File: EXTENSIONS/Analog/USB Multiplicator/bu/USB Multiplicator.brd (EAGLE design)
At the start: 30 x 63 mm, 9 parts, among them X1 USB-A

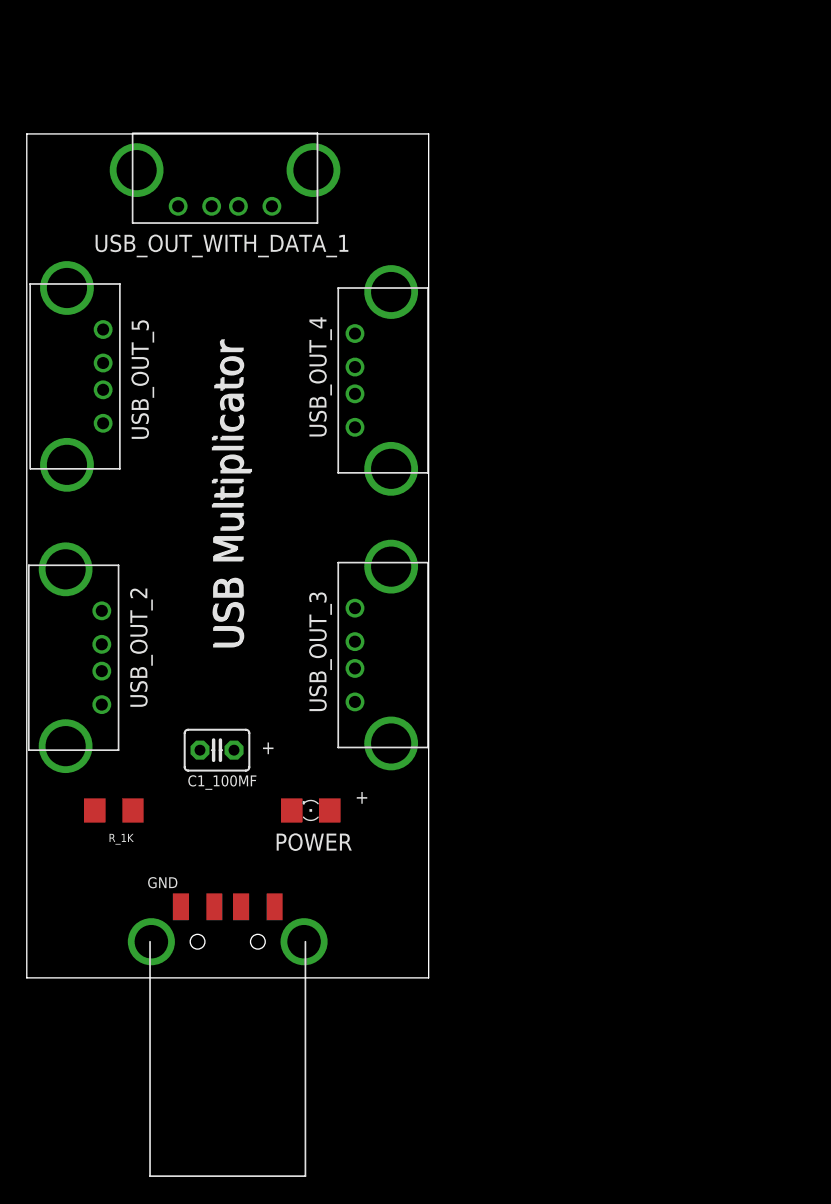
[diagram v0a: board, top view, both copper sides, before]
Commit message: Create v2 of USB Mutiplicator, make the board larger and 6 usb out
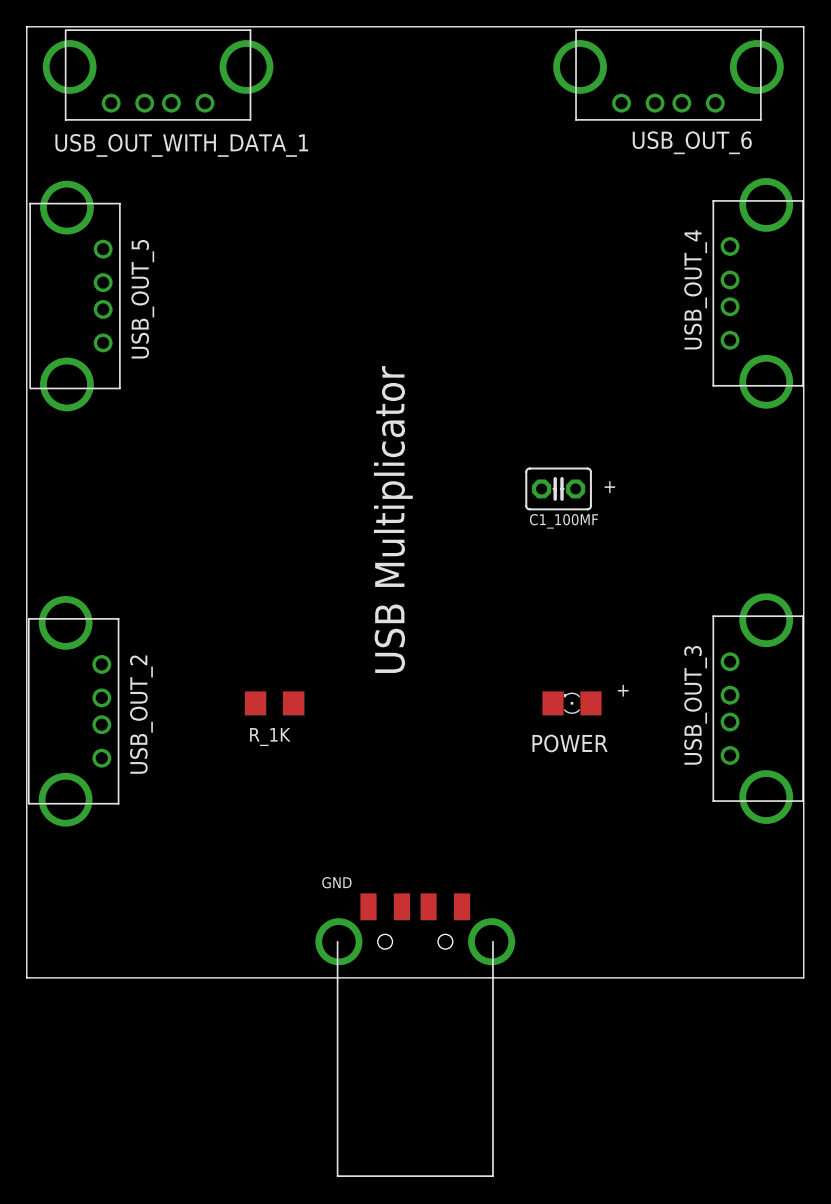
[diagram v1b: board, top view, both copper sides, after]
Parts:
- added USB_OUT_6: USB, STUNTAZ:USB-FEMALE-A-PTH
- moved C1_100MF 32.1 mm to (41.7, 48.5)
- moved USB_OUT_4 28.7 mm to (53.2, 70.0)
- moved USB_OUT_3 28.3 mm to (53.2, 39.0)
- moved LED_PWR 21.1 mm to (42.7, 32.5)
- moved R_1K 14.4 mm to (20.5, 32.5)
- moved X1 14.0 mm to (31.0, 14.7)
- moved USB_OUT_WITH_DATA_1 9.18 mm to (4.90, 76.0)
- moved USB_OUT_5 6.00 mm to (9.00, 56.0)
- moved USB_OUT_2 4.00 mm to (8.90, 25.0)
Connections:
- net GND: now also USB_OUT_6.GND
- net VCC: now also USB_OUT_6.VBUS
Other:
- board size 30 x 63 mm -> 58 x 71 mm
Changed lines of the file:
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@@
 <board>
 <plain>
-<wire x1="2" y1="12" x2="32" y2="12" width="0" layer="20"/>
-<wire x1="32" y1="12" x2="32" y2="75" width="0" layer="20"/>
-<wire x1="32" y1="75" x2="2" y2="75" width="0" layer="20"/>
-<wire x1="2" y1="75" x2="2" y2="12" width="0" layer="20"/>
+<wire x1="2" y1="12" x2="60" y2="12" width="0" layer="20"/>
+<wire x1="60" y1="12" x2="60" y2="83" width="0" layer="20"/>
+<wire x1="60" y1="83" x2="2" y2="83" width="0" layer="20"/>
+<wire x1="2" y1="83" x2="2" y2="12" width="0" layer="20"/>
 <text x="17" y="50.2" size="1.778" layer="26" rot="SMR90" align="center">USB Multiplicator
 MadeInTheUSB.net </text>
 <text x="22.5" y="18" size="1.27" layer="26" rot="MR90">PCBv2 - 2019.08</text>
-<text x="11" y="18.7" size="0.8128" layer="25">GND</text>
-<text x="19.5" y="28.7" size="1.016" layer="25">+</text>
-<text x="26.5" y="25" size="1.016" layer="25">+</text>
-<text x="20.5" y="21.5" size="1.27" layer="25">POWER</text>
-<text x="17" y="48" size="2.1844" layer="25" rot="R90" align="center">USB Multiplicator</text>
-<text x="17.1" y="48.1" size="2.1844" layer="25" rot="R90" align="center">USB Multiplicator</text>
+<text x="24" y="18.7" size="0.8128" layer="25">GND</text>
+<text x="45" y="48.2" size="1.016" layer="25">+</text>
+<text x="46" y="33" size="1.016" layer="25">+</text>
+<text x="42.5" y="29.5" size="1.27" layer="25" align="center">POWER</text>
+<text x="29.1" y="46.1" size="2.1844" layer="25" rot="R90" align="center">USB Multiplicator</text>
 </plain>
 <attributes>
@@
 </autorouter>
 <elements>
-<element name="X1" library="adafruit" package="MOLEX_480371000" value="USB-A" x="17" y="14.7" smashed="yes">
-<attribute name="VALUE" x="15.46" y="11.35" size="1.016" layer="27" font="vector"/>
-</element>
-<element name="C1_100MF" library="adafruit" package="C025-030X050" value="" x="16.2" y="29" smashed="yes">
-<attribute name="NAME" x="14" y="26.3" size="0.8128" layer="25" ratio="10"/>
-<attribute name="VALUE" x="13.914" y="25.952" size="1.27" layer="27" ratio="10"/>
-</element>
-<element name="LED_PWR" library="adafruit" package="1206" value="" x="23.2" y="24.5" smashed="yes" rot="R180">
-<attribute name="VALUE" x="24.47" y="27.04" size="1.27" layer="27" rot="R180"/>
-</element>
-<element name="R_1K" library="adafruit" package="R1206" value="" x="8.5" y="24.5" smashed="yes">
-<attribute name="NAME" x="8.103" y="22.143" size="0.6096" layer="25"/>
-<attribute name="VALUE" x="7.103" y="22.087" size="1.27" layer="27"/>
-</element>
-<element name="USB_OUT_WITH_DATA_1" library="STUNTAZ" package="USB-FEMALE-A-PTH" value="USB" x="9.9" y="68.3" smashed="yes">
-<attribute name="NAME" x="7" y="66.2" size="1.27" layer="25"/>
-</element>
-<element name="USB_OUT_2" library="STUNTAZ" package="USB-FEMALE-A-PTH" value="USB" x="8.9" y="29" smashed="yes" rot="R90">
-<attribute name="NAME" x="11" y="32.1" size="1.27" layer="25" rot="R90"/>
-</element>
-<element name="USB_OUT_3" library="STUNTAZ" package="USB-FEMALE-A-PTH" value="USB" x="25.2" y="43" smashed="yes" rot="R270">
-<attribute name="NAME" x="23.1" y="40.9" size="1.27" layer="25" rot="R270"/>
-</element>
-<element name="USB_OUT_4" library="STUNTAZ" package="USB-FEMALE-A-PTH" value="USB" x="25.2" y="63.5" smashed="yes" rot="R270">
-<attribute name="NAME" x="23.1" y="61.4" size="1.27" layer="25" rot="R270"/>
-</element>
-<element name="USB_OUT_5" library="STUNTAZ" package="USB-FEMALE-A-PTH" value="USB" x="9" y="50" smashed="yes" rot="R90">
-<attribute name="NAME" x="11.1" y="52.1" size="1.27" layer="25" rot="R90"/>
-</element>
+<element name="X1" library="adafruit" package="MOLEX_480371000" value="USB-A" x="31" y="14.7" smashed="yes">
+<attribute name="VALUE" x="29.46" y="11.35" size="1.016" layer="27" font="vector"/>
+</element>
+<element name="C1_100MF" library="adafruit" package="C025-030X050" value="" x="41.7" y="48.5" smashed="yes">
+<attribute name="NAME" x="39.5" y="45.8" size="0.8128" layer="25" ratio="10"/>
+<attribute name="VALUE" x="39.414" y="45.452" size="1.27" layer="27" ratio="10"/>
+</element>
+<element name="LED_PWR" library="adafruit" package="1206" value="" x="42.7" y="32.5" smashed="yes" rot="R180">
+<attribute name="VALUE" x="43.97" y="35.04" size="1.27" layer="27" rot="R180"/>
+</element>
+<element name="R_1K" library="adafruit" package="R1206" value="" x="20.5" y="32.5" smashed="yes">
+<attribute name="NAME" x="20.103" y="30.143" size="1.016" layer="25" align="center"/>
+<attribute name="VALUE" x="19.103" y="30.087" size="1.27" layer="27"/>
+</element>
+<element name="USB_OUT_WITH_DATA_1" library="STUNTAZ" package="USB-FEMALE-A-PTH" value="USB" x="4.9" y="76" smashed="yes">
+<attribute name="NAME" x="4" y="73.7" size="1.27" layer="25"/>
+</element>
+<element name="USB_OUT_2" library="STUNTAZ" package="USB-FEMALE-A-PTH" value="USB" x="8.9" y="25" smashed="yes" rot="R90">
+<attribute name="NAME" x="11" y="27.1" size="1.27" layer="25" rot="R90"/>
+</element>
+<element name="USB_OUT_3" library="STUNTAZ" package="USB-FEMALE-A-PTH" value="USB" x="53.2" y="39" smashed="yes" rot="R270">
+<attribute name="NAME" x="51.1" y="36.9" size="1.27" layer="25" rot="R270"/>
+</element>
+<element name="USB_OUT_4" library="STUNTAZ" package="USB-FEMALE-A-PTH" value="USB" x="53.2" y="70" smashed="yes" rot="R270">
+<attribute name="NAME" x="51.1" y="67.9" size="1.27" layer="25" rot="R270"/>
+</element>
+<element name="USB_OUT_5" library="STUNTAZ" package="USB-FEMALE-A-PTH" value="USB" x="9" y="56" smashed="yes" rot="R90">
+<attribute name="NAME" x="11.1" y="58.1" size="1.27" layer="25" rot="R90"/>
+</element>
+<element name="USB_OUT_6" library="STUNTAZ" package="USB-FEMALE-A-PTH" value="USB" x="43" y="76"/>
 </elements>
 <signals>
@@
 <contactref element="USB_OUT_4" pad="GND"/>
 <contactref element="USB_OUT_5" pad="GND"/>
-<wire x1="13.3" y1="69.6" x2="26.5" y2="60.1" width="0" layer="19" extent="1-1"/>
-<wire x1="7.7" y1="53.4" x2="13.3" y2="69.6" width="0" layer="19" extent="1-1"/>
-<wire x1="26.5" y1="39.6" x2="26.5" y2="60.1" width="0" layer="19" extent="1-1"/>
-<wire x1="14.93" y1="29" x2="26.5" y2="39.6" width="0" layer="19" extent="1-1"/>
-<wire x1="7.6" y1="32.4" x2="14.93" y2="29" width="0" layer="19" extent="1-1"/>
-<wire x1="7.078" y1="24.5" x2="7.6" y2="32.4" width="0" layer="19" extent="1-1"/>
-<wire x1="13.5" y1="17.3" x2="7.078" y2="24.5" width="0" layer="19" extent="1-1"/>
+<contactref element="USB_OUT_6" pad="GND"/>
+<wire x1="54.5" y1="66.6" x2="46.4" y2="77.3" width="0" layer="19" extent="1-1"/>
+<wire x1="54.5" y1="35.6" x2="54.5" y2="66.6" width="0" layer="19" extent="1-1"/>
+<wire x1="27.5" y1="17.3" x2="54.5" y2="35.6" width="0" layer="19" extent="1-1"/>
+<wire x1="40.43" y1="48.5" x2="27.5" y2="17.3" width="0" layer="19" extent="1-1"/>
+<wire x1="7.6" y1="28.4" x2="40.43" y2="48.5" width="0" layer="19" extent="1-1"/>
+<wire x1="19.078" y1="32.5" x2="7.6" y2="28.4" width="0" layer="19" extent="1-1"/>
+<wire x1="7.7" y1="59.4" x2="7.6" y2="28.4" width="0" layer="19" extent="1-1"/>
+<wire x1="8.3" y1="77.3" x2="7.7" y2="59.4" width="0" layer="19" extent="1-1"/>
 </signal>
 <signal name="VCC">
@@
 <contactref element="USB_OUT_4" pad="VBUS"/>
 <contactref element="USB_OUT_5" pad="VBUS"/>
-<wire x1="7.7" y1="60.4" x2="20.3" y2="69.6" width="0" layer="19" extent="1-1"/>
-<wire x1="26.5" y1="53.1" x2="20.3" y2="69.6" width="0" layer="19" extent="1-1"/>
-<wire x1="26.5" y1="32.6" x2="26.5" y2="53.1" width="0" layer="19" extent="1-1"/>
-<wire x1="24.622" y1="24.5" x2="26.5" y2="32.6" width="0" layer="19" extent="1-1"/>
-<wire x1="20.5" y1="17.3" x2="24.622" y2="24.5" width="0" layer="19" extent="1-1"/>
-<wire x1="17.47" y1="29" x2="24.622" y2="24.5" width="0" layer="19" extent="1-1"/>
-<wire x1="7.6" y1="39.4" x2="17.47" y2="29" width="0" layer="19" extent="1-1"/>
+<contactref element="USB_OUT_6" pad="VBUS"/>
+<wire x1="54.5" y1="59.6" x2="53.4" y2="77.3" width="0" layer="19" extent="1-1"/>
+<wire x1="54.5" y1="28.6" x2="54.5" y2="59.6" width="0" layer="19" extent="1-1"/>
+<wire x1="34.5" y1="17.3" x2="54.5" y2="28.6" width="0" layer="19" extent="1-1"/>
+<wire x1="44.122" y1="32.5" x2="34.5" y2="17.3" width="0" layer="19" extent="1-1"/>
+<wire x1="42.97" y1="48.5" x2="44.122" y2="32.5" width="0" layer="19" extent="1-1"/>
+<wire x1="7.6" y1="35.4" x2="42.97" y2="48.5" width="0" layer="19" extent="1-1"/>
+<wire x1="7.7" y1="66.4" x2="7.6" y2="35.4" width="0" layer="19" extent="1-1"/>
+<wire x1="15.3" y1="77.3" x2="7.7" y2="66.4" width="0" layer="19" extent="1-1"/>
 </signal>
 <signal name="N$5">
 <contactref element="LED_PWR" pad="C"/>
 <contactref element="R_1K" pad="2"/>
-<wire x1="9.922" y1="24.5" x2="21.778" y2="24.5" width="0" layer="19" extent="1-1"/>
+<wire x1="21.922" y1="32.5" x2="41.278" y2="32.5" width="0" layer="19" extent="1-1"/>
 </signal>
 <signal name="USB_DPLUS">
 <contactref element="X1" pad="3"/>
 <contactref element="USB_OUT_WITH_DATA_1" pad="D-"/>
-<wire x1="16" y1="17.3" x2="17.8" y2="69.6" width="0" layer="19" extent="1-1"/>
+<wire x1="30" y1="17.3" x2="12.8" y2="77.3" width="0" layer="19" extent="1-1"/>
 </signal>
 <signal name="USB_DMINUS">
 <contactref element="X1" pad="2"/>
 <contactref element="USB_OUT_WITH_DATA_1" pad="D+"/>
-<wire x1="18" y1="17.3" x2="15.8" y2="69.6" width="0" layer="19" extent="1-1"/>
+<wire x1="32" y1="17.3" x2="10.8" y2="77.3" width="0" layer="19" extent="1-1"/>
 </signal>
 </signals>

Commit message: Create USB multiplicator v2 big
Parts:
- moved USB_OUT_3 7.00 mm to (53.2, 32.0)
- moved USB_OUT_2 6.00 mm to (8.90, 19.0)
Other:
- board text added: "PCBv3 - 2019.12"
- board text removed: "PCBv2 - 2019.08"
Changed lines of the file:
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@@
 <wire x1="60" y1="83" x2="2" y2="83" width="0" layer="20"/>
 <wire x1="2" y1="83" x2="2" y2="12" width="0" layer="20"/>
-<text x="17" y="50.2" size="1.778" layer="26" rot="SMR90" align="center">USB Multiplicator
+<text x="31" y="55.2" size="3.81" layer="26" rot="SMR90" align="center">USB Multiplicator
 MadeInTheUSB.net </text>
-<text x="22.5" y="18" size="1.27" layer="26" rot="MR90">PCBv2 - 2019.08</text>
+<text x="30.5" y="23" size="1.27" layer="26" rot="MR0" align="center">PCBv3 - 2019.12</text>
 <text x="24" y="18.7" size="0.8128" layer="25">GND</text>
 <text x="45" y="48.2" size="1.016" layer="25">+</text>
 <text x="46" y="33" size="1.016" layer="25">+</text>
 <text x="42.5" y="29.5" size="1.27" layer="25" align="center">POWER</text>
-<text x="29.1" y="46.1" size="2.1844" layer="25" rot="R90" align="center">USB Multiplicator</text>
+<text x="31.1" y="49.1" size="3.81" layer="25" rot="R90" align="center">USB Multiplicator</text>
 </plain>
 <attributes>
@@
 </element>
 <element name="C1_100MF" library="adafruit" package="C025-030X050" value="" x="41.7" y="48.5" smashed="yes">
-<attribute name="NAME" x="39.5" y="45.8" size="0.8128" layer="25" ratio="10"/>
+<attribute name="NAME" x="41.5" y="45.8" size="1.27" layer="25" ratio="10" align="center"/>
 <attribute name="VALUE" x="39.414" y="45.452" size="1.27" layer="27" ratio="10"/>
 </element>
@@
 <attribute name="NAME" x="4" y="73.7" size="1.27" layer="25"/>
 </element>
-<element name="USB_OUT_2" library="STUNTAZ" package="USB-FEMALE-A-PTH" value="USB" x="8.9" y="25" smashed="yes" rot="R90">
-<attribute name="NAME" x="11" y="27.1" size="1.27" layer="25" rot="R90"/>
-</element>
-<element name="USB_OUT_3" library="STUNTAZ" package="USB-FEMALE-A-PTH" value="USB" x="53.2" y="39" smashed="yes" rot="R270">
-<attribute name="NAME" x="51.1" y="36.9" size="1.27" layer="25" rot="R270"/>
+<element name="USB_OUT_2" library="STUNTAZ" package="USB-FEMALE-A-PTH" value="USB" x="8.9" y="19" smashed="yes" rot="R90">
+<attribute name="NAME" x="11" y="21.1" size="1.27" layer="25" rot="R90"/>
+</element>
+<element name="USB_OUT_3" library="STUNTAZ" package="USB-FEMALE-A-PTH" value="USB" x="53.2" y="32" smashed="yes" rot="R270">
+<attribute name="NAME" x="51.1" y="29.9" size="1.27" layer="25" rot="R270"/>
 </element>
 <element name="USB_OUT_4" library="STUNTAZ" package="USB-FEMALE-A-PTH" value="USB" x="53.2" y="70" smashed="yes" rot="R270">
@@
 <contactref element="USB_OUT_6" pad="GND"/>
 <wire x1="54.5" y1="66.6" x2="46.4" y2="77.3" width="0" layer="19" extent="1-1"/>
-<wire x1="54.5" y1="35.6" x2="54.5" y2="66.6" width="0" layer="19" extent="1-1"/>
-<wire x1="27.5" y1="17.3" x2="54.5" y2="35.6" width="0" layer="19" extent="1-1"/>
-<wire x1="40.43" y1="48.5" x2="27.5" y2="17.3" width="0" layer="19" extent="1-1"/>
-<wire x1="7.6" y1="28.4" x2="40.43" y2="48.5" width="0" layer="19" extent="1-1"/>
-<wire x1="19.078" y1="32.5" x2="7.6" y2="28.4" width="0" layer="19" extent="1-1"/>
-<wire x1="7.7" y1="59.4" x2="7.6" y2="28.4" width="0" layer="19" extent="1-1"/>
+<wire x1="40.43" y1="48.5" x2="54.5" y2="66.6" width="0" layer="19" extent="1-1"/>
+<wire x1="54.5" y1="28.6" x2="40.43" y2="48.5" width="0" layer="19" extent="1-1"/>
+<wire x1="19.078" y1="32.5" x2="40.43" y2="48.5" width="0" layer="19" extent="1-1"/>
+<wire x1="7.6" y1="22.4" x2="19.078" y2="32.5" width="0" layer="19" extent="1-1"/>
+<wire x1="27.5" y1="17.3" x2="19.078" y2="32.5" width="0" layer="19" extent="1-1"/>
+<wire x1="7.7" y1="59.4" x2="19.078" y2="32.5" width="0" layer="19" extent="1-1"/>
 <wire x1="8.3" y1="77.3" x2="7.7" y2="59.4" width="0" layer="19" extent="1-1"/>
 </signal>
@@
 <contactref element="USB_OUT_6" pad="VBUS"/>
 <wire x1="54.5" y1="59.6" x2="53.4" y2="77.3" width="0" layer="19" extent="1-1"/>
-<wire x1="54.5" y1="28.6" x2="54.5" y2="59.6" width="0" layer="19" extent="1-1"/>
-<wire x1="34.5" y1="17.3" x2="54.5" y2="28.6" width="0" layer="19" extent="1-1"/>
-<wire x1="44.122" y1="32.5" x2="34.5" y2="17.3" width="0" layer="19" extent="1-1"/>
-<wire x1="42.97" y1="48.5" x2="44.122" y2="32.5" width="0" layer="19" extent="1-1"/>
-<wire x1="7.6" y1="35.4" x2="42.97" y2="48.5" width="0" layer="19" extent="1-1"/>
-<wire x1="7.7" y1="66.4" x2="7.6" y2="35.4" width="0" layer="19" extent="1-1"/>
+<wire x1="42.97" y1="48.5" x2="54.5" y2="59.6" width="0" layer="19" extent="1-1"/>
+<wire x1="44.122" y1="32.5" x2="42.97" y2="48.5" width="0" layer="19" extent="1-1"/>
+<wire x1="54.5" y1="21.6" x2="44.122" y2="32.5" width="0" layer="19" extent="1-1"/>
+<wire x1="34.5" y1="17.3" x2="44.122" y2="32.5" width="0" layer="19" extent="1-1"/>
+<wire x1="7.6" y1="29.4" x2="34.5" y2="17.3" width="0" layer="19" extent="1-1"/>
+<wire x1="7.7" y1="66.4" x2="7.6" y2="29.4" width="0" layer="19" extent="1-1"/>
 <wire x1="15.3" y1="77.3" x2="7.7" y2="66.4" width="0" layer="19" extent="1-1"/>
 </signal>
